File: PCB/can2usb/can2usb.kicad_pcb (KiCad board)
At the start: 2 copper layers, 39 parts, among them J1 STLINK, J2 Conn_01x03_Male, P1 USB_C_Plug_USB2.0, U1 STM32F103C6Tx, U2 TLP175A, U3 MCP2561-E-SN, U5 USBLC6-2SC6, U6 MIC5528-3.3YMT-TR, Y1 16MHz, Y2 32KHz

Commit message: New PCB design
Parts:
- added H4: MountingHole, MountingHole:MountingHole_2.2mm_M2, F.Cu at (112.3, 73.1)
- C5, C6, C7, C8, R_Terminator1: moved to B.Cu
- moved Y1 53.3 mm to (130.4, 90.9)
- moved Y2 46.7 mm to (127.8, 87.4), turned to 180 degrees
- moved R5 45.5 mm to (125.5, 90.6), turned to 180 degrees
- moved R4 43.3 mm to (127.4, 84.8)
- moved C6 41.2 mm to (134.3, 86.6), turned to 45 degrees
- moved J2 41.0 mm to (116.2, 79.8)
- moved U2 39.9 mm to (119.9, 89.3), turned to 180 degrees
- moved C5 39.9 mm to (133.5, 85.7), turned to 45 degrees
- moved D3 38.1 mm to (123.8, 85.5), turned to 180 degrees
- moved C8 37.0 mm to (133.3, 83.8), turned to 45 degrees
- moved C7 33.4 mm to (132.6, 83.0), turned to 45 degrees
- moved R_Terminator1 30.7 mm to (119.1, 87.5), turned to 180 degrees
- moved H3 26.0 mm to (112.3, 91.1)
- moved H2 3.31 mm to (148.3, 73.1)
- moved H1 3.20 mm to (148.3, 91.1)
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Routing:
- net GND: track 103.6 -> 124.2 mm, vias 6 -> 8
- net CAN_L: track 0.00 -> 18.9 mm, vias 0 -> 1
- net TERMINATOR_SW: track 0.00 -> 16.2 mm, vias 0 -> 2
- net CAN_H: track 0.00 -> 15.4 mm, vias 0 -> 2
- net OSC_IN: track 0.00 -> 10.6 mm, vias 0 -> 1
- net L_OSC_IN: track 0.00 -> 10.2 mm, vias 0 -> 1
- net OSC_OUT: track 0.00 -> 8.90 mm, vias 0 -> 1
- net L_OSC_OUT: track 0.00 -> 7.67 mm, vias 0 -> 1
- net +5V: track 44.5 -> 37.3 mm, vias 1 -> 2
- net Net-(R_Terminator1-Pad2): track 0.00 -> 3.79 mm, vias 0 -> 1
- net B_LED: track 0.00 -> 2.99 mm
- net Net-(D3-Pad1): track 0.00 -> 2.37 mm
- net Net-(R5-Pad2): track 0.00 -> 1.88 mm
- net +3V3: track 72.1 -> 73.6 mm, vias 6 -> 5
- net Net-(JP1-Pad2): track 4.56 -> 3.29 mm
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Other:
- board outline added: 50.3 x 22.1 mm
- rule trace_min: 0.2 -> 0.1
- board text added: "CAN.H"
- board text added: "CAN.L"
- board text added: "GND"
- board text added: "SYS"
- board text added: "USB2CAN"
- board text added: "by K.Pergol"

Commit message: Minor changes in PCB desing
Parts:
- moved R2 3.78 mm to (141.4, 87.5)
- moved R3 3.33 mm to (141.5, 85.9), turned to 180 degrees
- moved D2 1.40 mm to (144.9, 84.3)
- moved H2 0.85 mm to (147.7, 73.7)
- moved H1 0.85 mm to (147.7, 90.5)
- moved H4 0.85 mm to (112.9, 73.7)
- moved H3 0.85 mm to (112.9, 90.5)
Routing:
- net CAN_LED: track 7.48 -> 3.42 mm
- net UART_LED: track 7.65 -> 3.66 mm
- net GND: track 124.2 -> 122.5 mm, vias 8 -> 7
- net Net-(D2-Pad1): track 2.01 -> 2.85 mm
- net Net-(D1-Pad1): track 2.49 -> 1.86 mm

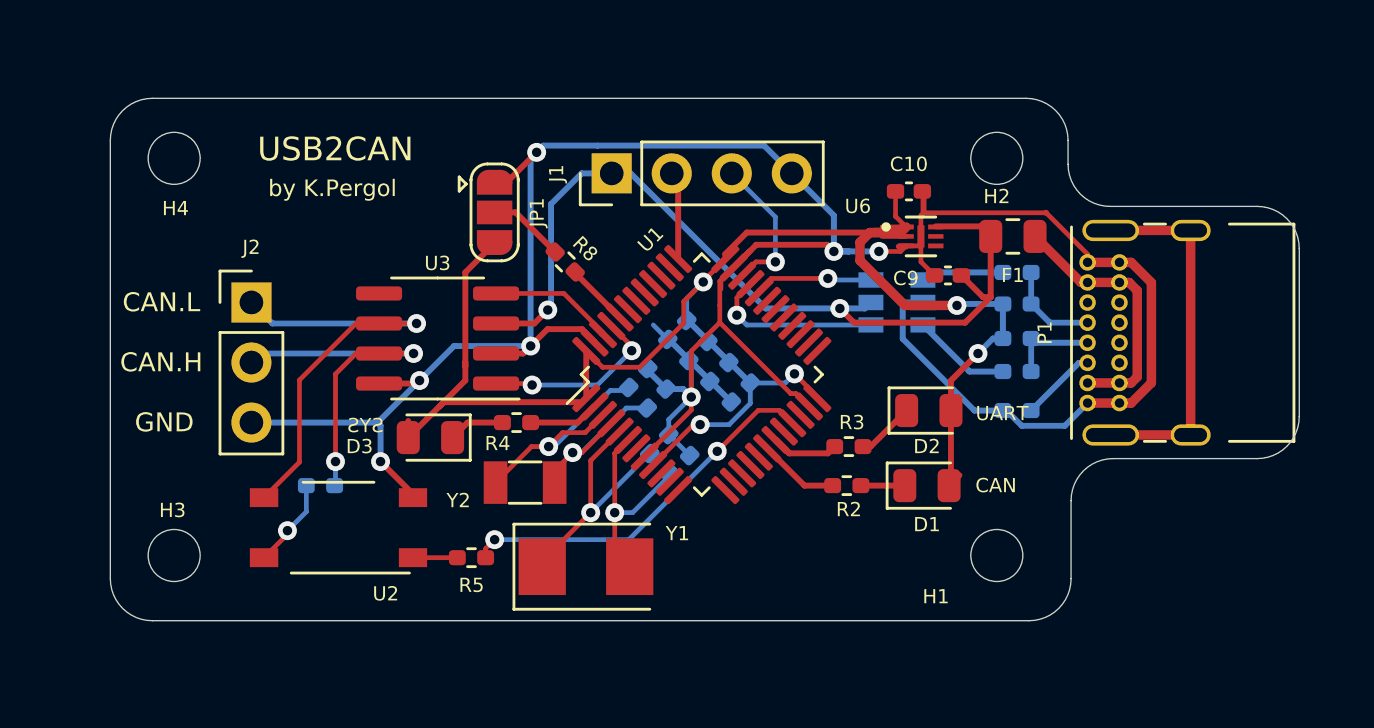
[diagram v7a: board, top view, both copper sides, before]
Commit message: PCB modifications after production
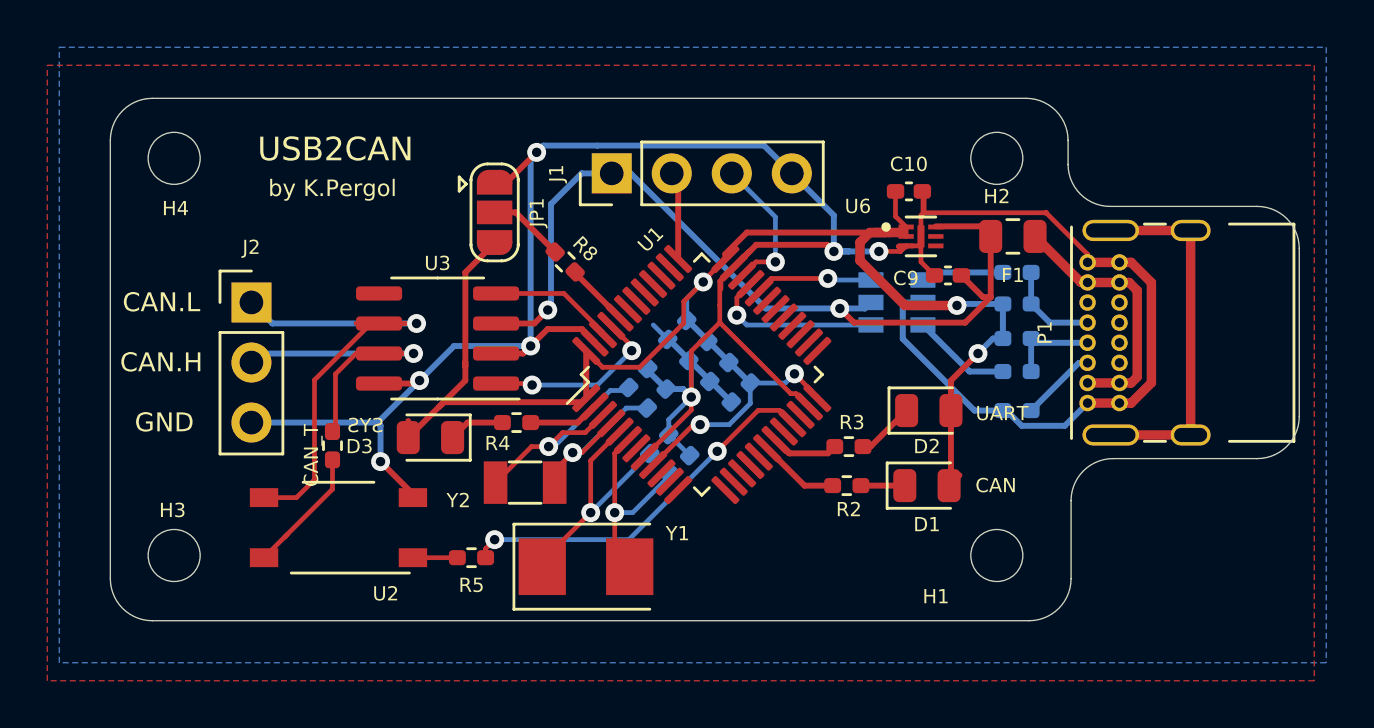
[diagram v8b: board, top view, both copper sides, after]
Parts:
- CAN_T: renamed from R_Terminator1; moved to F.Cu
- moved CAN_T 1.76 mm to (119.6, 85.8), turned to -90 degrees
- renumbered R_CONF1 to RCF1, R_CONF2 to RCF2
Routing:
- net CAN_H: track 15.4 -> 13.2 mm, vias 2 -> 1
- net Net-(R_Terminator1-Pad2): track 3.79 -> 5.50 mm, vias 1 -> 0
- net CAN_L: track 18.9 -> 20.3 mm
- net +3V3: track 73.7 -> 73.0 mm
- added copper zone on F.Cu, net (none)
- added copper zone on B.Cu, net GND
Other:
- net class Default removed
- net class Small removed
